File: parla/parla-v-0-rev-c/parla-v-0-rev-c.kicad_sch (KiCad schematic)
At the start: 21 parts, among them J1 AudioJack2_SwitchT, J2 AudioJack2_SwitchT, J3 AudioJack2_SwitchT, J4 AudioJack2_SwitchT, J6 Conn_02x05_Odd_Even, U1 PAM8403D, U2 L7805

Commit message: agregar parla v0-rev-c
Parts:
- removed C7: 100n, symbol Device:C
- added C10: 100n, Capacitor_SMD:C_0805_2012Metric_Pad1.18x1.45mm_HandSolder, symbol Device:C
- added C9: 10u, Capacitor_SMD:CP_Elec_4x5.4, symbol Device:C_Polarized
- D2, D3: value 1N5817 -> D_Schottky; footprint (none) -> easyeda2kicad:SOD-123FL_L2.8-W1.8-LS3.7-R-RD
- RV1, RV2: footprint BYOM_General:Potentiometer_Bourns_3296W_Vertical -> BYOM_General:POT_TH_Alps_RK09K_Single_Vertical
- U2: footprint (none) -> Package_TO_SOT_SMD:TO-252-2; LCSC (none) -> C19626525
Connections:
- net +5V: now also C10.1, C9.1
- net GND: now also C10.2, C9.2

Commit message: agregar mas avances en eurorack
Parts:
- removed C4, C5, C6: 1u, Capacitor_SMD:C_0805_2012Metric_Pad1.18x1.45mm_HandSolder, symbol Device:C
- renumbered C9 to C4, C10 to C5, C8 to C6, D3 to D1, J6 to J1, J3 to J2, J4 to J3, J1 to J4, J2 to J5, R3 to R1, R4 to R2, U2 to U1, U1 to U2
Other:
- moved on the sheet: C6

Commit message: cambiar conector
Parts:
- J1: footprint Connector_IDC:IDC-Header_2x05_P2.54mm_Vertical -> BYOM_General:IDC-Header_2x05_P2.54mm_Vertical
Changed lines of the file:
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@@
 			)
 		)
-		(property "Footprint" "Connector_IDC:IDC-Header_2x05_P2.54mm_Vertical"
+		(property "Footprint" "BYOM_General:IDC-Header_2x05_P2.54mm_Vertical"
 			(at 36.83 163.83 0)
 			(hide yes)

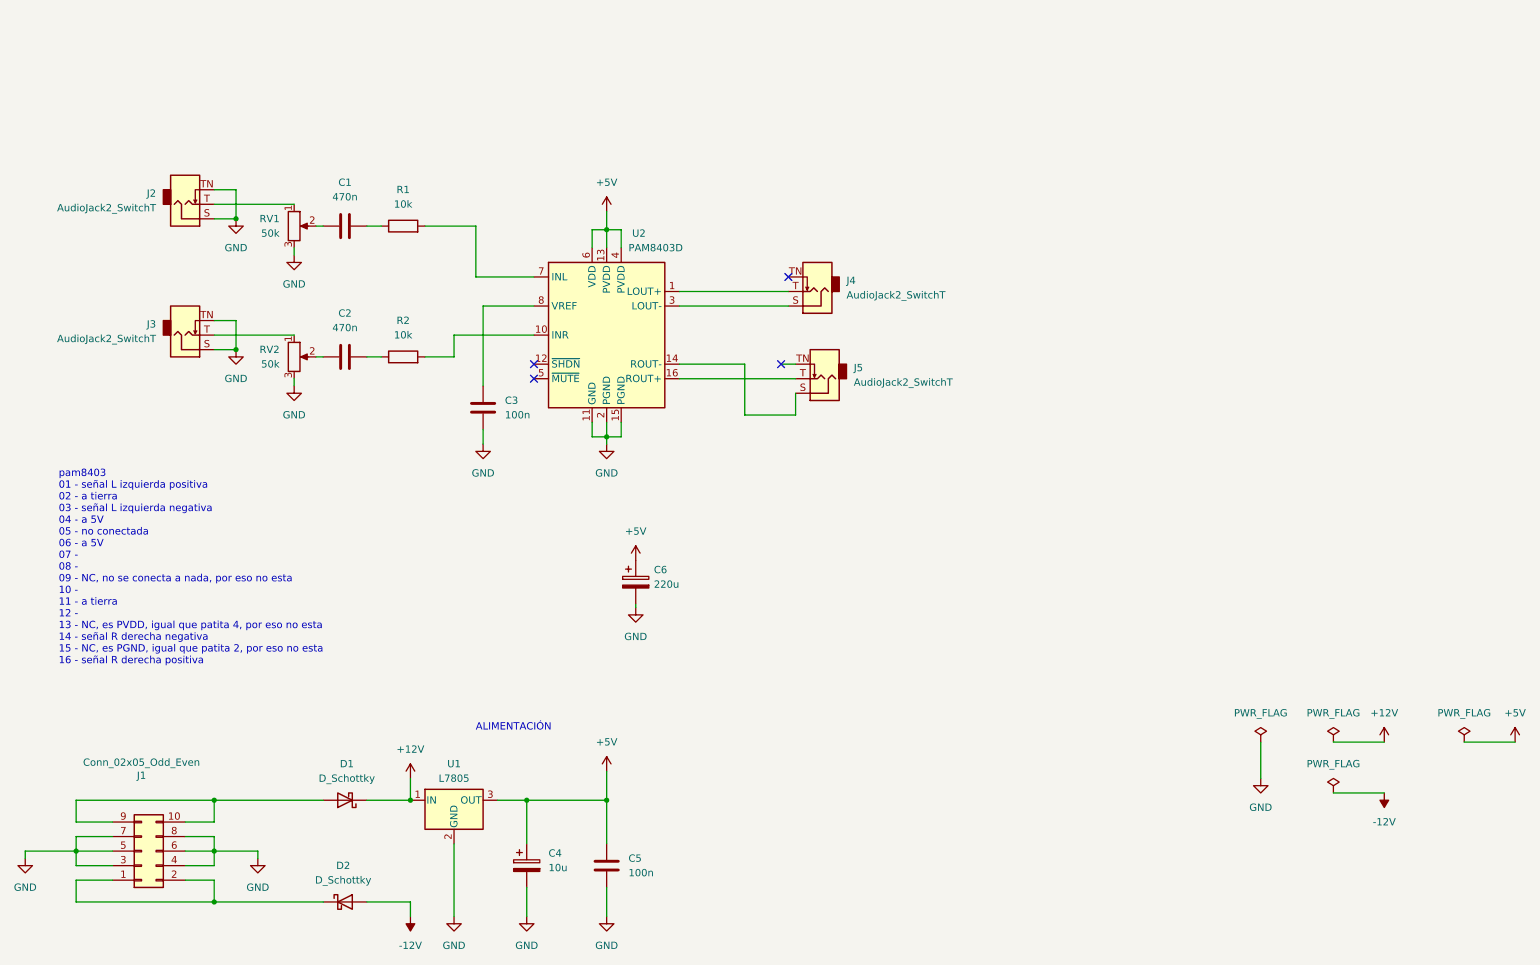
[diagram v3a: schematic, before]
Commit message: renombrar a versiones consistentes
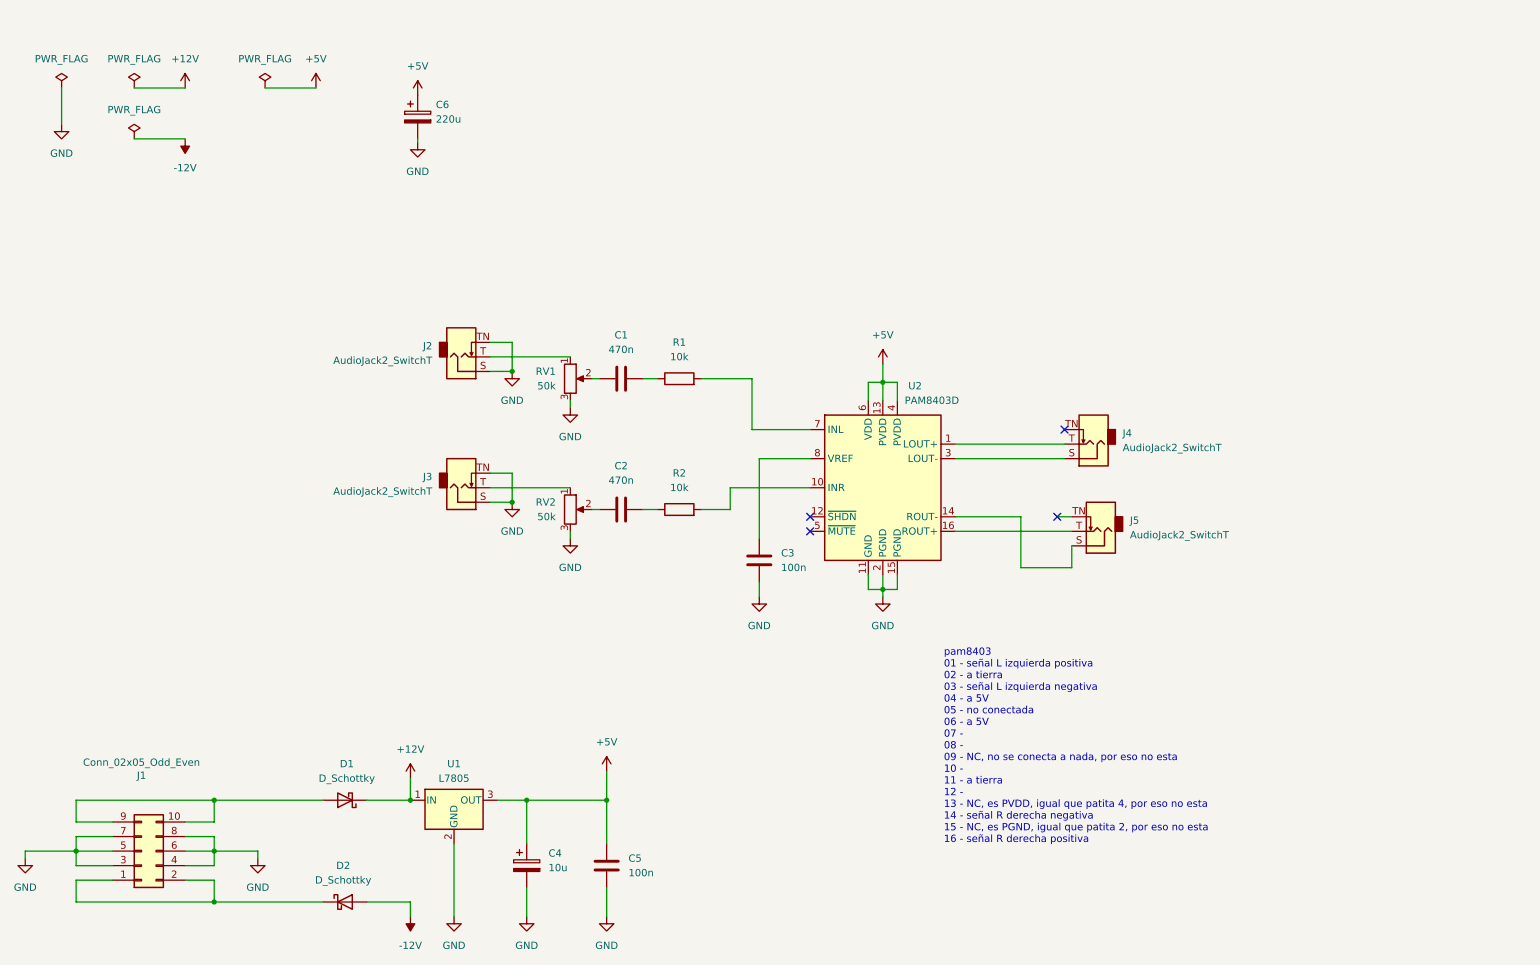
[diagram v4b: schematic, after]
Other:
- note removed: "ALIMENTACIÓN"
- moved on the sheet: C1, C2, C3, C6, J2, J3, J4, J5, R1, R2, RV1, RV2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

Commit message: agregar parla relo ataconso con bibliotecas locales
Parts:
- D1, D2: footprint easyeda2kicad:SOD-123FL_L2.8-W1.8-LS3.7-R-RD -> parla-v-0-rev-c:SOD-123FL_L2.8-W1.8-LS3.7-R-RD
- J1: footprint BYOM_General:IDC-Header_2x05_P2.54mm_Vertical -> parla-v-0-rev-c:IDC-Header_2x05_P2.54mm_Vertical
- J2, J3, J4, J5: footprint BYOM_General:Jack_3.5mm_QingPu_WQP-PJ398SM_Vertical -> parla-v-0-rev-c:Jack_3.5mm_QingPu_WQP-PJ398SM_Vertical
- RV1, RV2: footprint BYOM_General:POT_TH_Alps_RK09K_Single_Vertical -> parla-v-0-rev-c:POT_TH_Alps_RK09K_Single_Vertical
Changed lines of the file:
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@@
 			)
 		)
-		(property "Footprint" "BYOM_General:IDC-Header_2x05_P2.54mm_Vertical"
+		(property "Footprint" "parla-v-0-rev-c:IDC-Header_2x05_P2.54mm_Vertical"
 			(at 36.83 163.83 0)
 			(hide yes)
@@
 			)
 		)
-		(property "Footprint" "easyeda2kicad:SOD-123FL_L2.8-W1.8-LS3.7-R-RD"
+		(property "Footprint" "parla-v-0-rev-c:SOD-123FL_L2.8-W1.8-LS3.7-R-RD"
 			(at 72.39 172.72 0)
 			(hide yes)
@@
 			)
 		)
-		(property "Footprint" "easyeda2kicad:SOD-123FL_L2.8-W1.8-LS3.7-R-RD"
+		(property "Footprint" "parla-v-0-rev-c:SOD-123FL_L2.8-W1.8-LS3.7-R-RD"
 			(at 72.39 154.94 0)
 			(hide yes)
@@
 			)
 		)
-		(property "Footprint" "BYOM_General:Jack_3.5mm_QingPu_WQP-PJ398SM_Vertical"
+		(property "Footprint" "parla-v-0-rev-c:Jack_3.5mm_QingPu_WQP-PJ398SM_Vertical"
 			(at 92.71 77.47 0)
 			(hide yes)
@@
 			)
 		)
-		(property "Footprint" "BYOM_General:Jack_3.5mm_QingPu_WQP-PJ398SM_Vertical"
+		(property "Footprint" "parla-v-0-rev-c:Jack_3.5mm_QingPu_WQP-PJ398SM_Vertical"
 			(at 204.47 107.95 0)
 			(hide yes)
@@
 			)
 		)
-		(property "Footprint" "BYOM_General:Jack_3.5mm_QingPu_WQP-PJ398SM_Vertical"
+		(property "Footprint" "parla-v-0-rev-c:Jack_3.5mm_QingPu_WQP-PJ398SM_Vertical"
 			(at 203.2 92.71 0)
 			(hide yes)
@@
 			)
 		)
-		(property "Footprint" "BYOM_General:Jack_3.5mm_QingPu_WQP-PJ398SM_Vertical"
+		(property "Footprint" "parla-v-0-rev-c:Jack_3.5mm_QingPu_WQP-PJ398SM_Vertical"
 			(at 92.71 100.33 0)
 			(hide yes)
@@
 			)
 		)
-		(property "Footprint" "BYOM_General:POT_TH_Alps_RK09K_Single_Vertical"
+		(property "Footprint" "parla-v-0-rev-c:POT_TH_Alps_RK09K_Single_Vertical"
 			(at 111.76 104.14 0)
 			(hide yes)
@@
 			)
 		)
-		(property "Footprint" "BYOM_General:POT_TH_Alps_RK09K_Single_Vertical"
+		(property "Footprint" "parla-v-0-rev-c:POT_TH_Alps_RK09K_Single_Vertical"
 			(at 111.76 81.28 0)
 			(hide yes)
